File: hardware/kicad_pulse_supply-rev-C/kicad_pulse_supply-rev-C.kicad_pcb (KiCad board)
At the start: 4 copper layers, 127 x 96.5 mm, 179 parts, among them J1 USB_B_Micro, J2 SIG_EXT, J3 OPT_PWR, Q1 MMBT2222*, Q2 MMBT2222*, Q3 GAN7R0-150LBE, SW1 KMR211GLFS, U1 AP2112K-3.3, U10 LTC6244CMS8, U11 LTC6244CMS8, U12 TPS552892RYQR, U2 ESP32-WROOM-32D, U3 CP2104, U4 MAX4378, U5 UCC27611DRVT, U6 MCP1703T-5002E/MB, U7 LTC6244CMS8, U8 LTC6244CMS8, U9 LTC6244CMS8

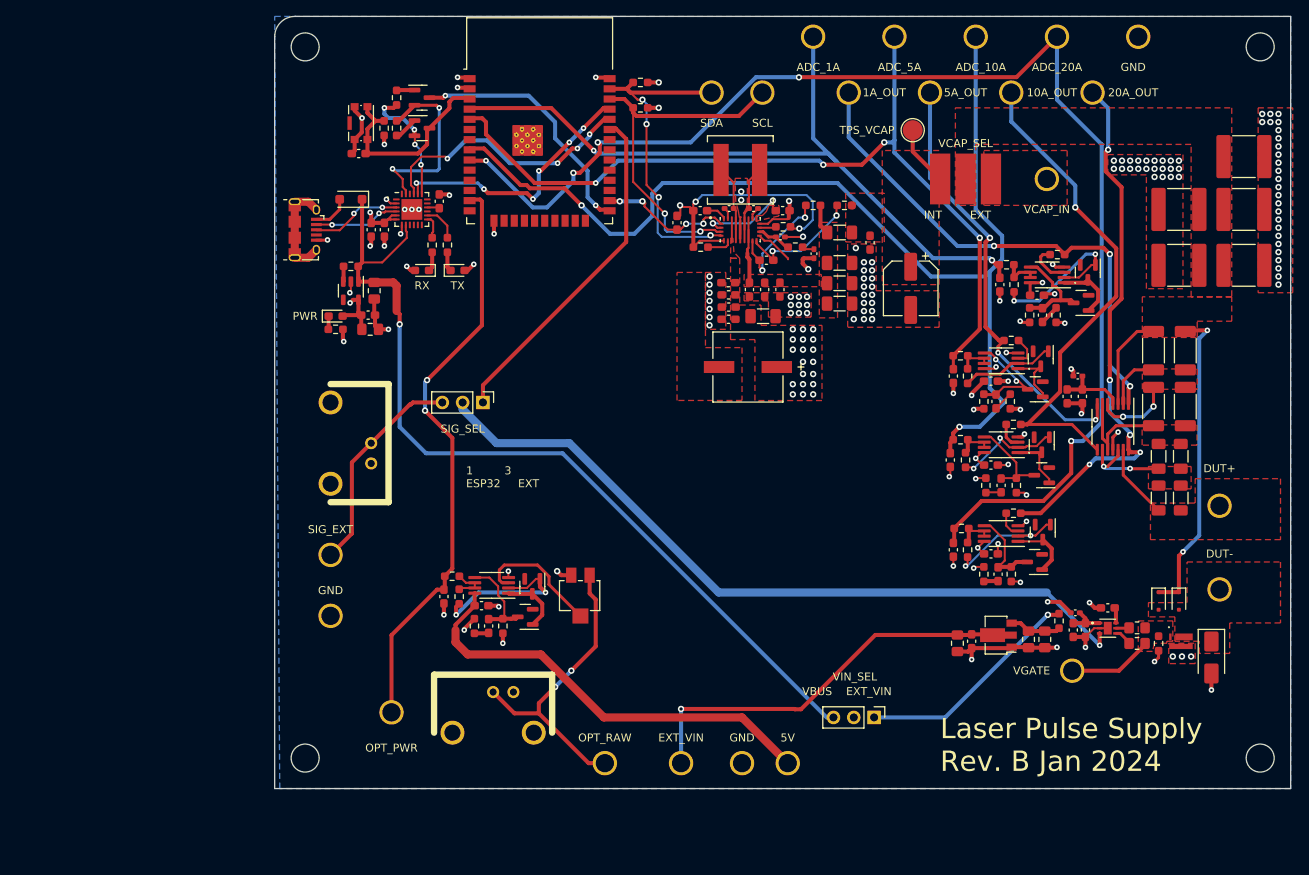
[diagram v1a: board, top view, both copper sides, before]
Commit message: Rev C pcb complete, last commit before branching firmware for new board
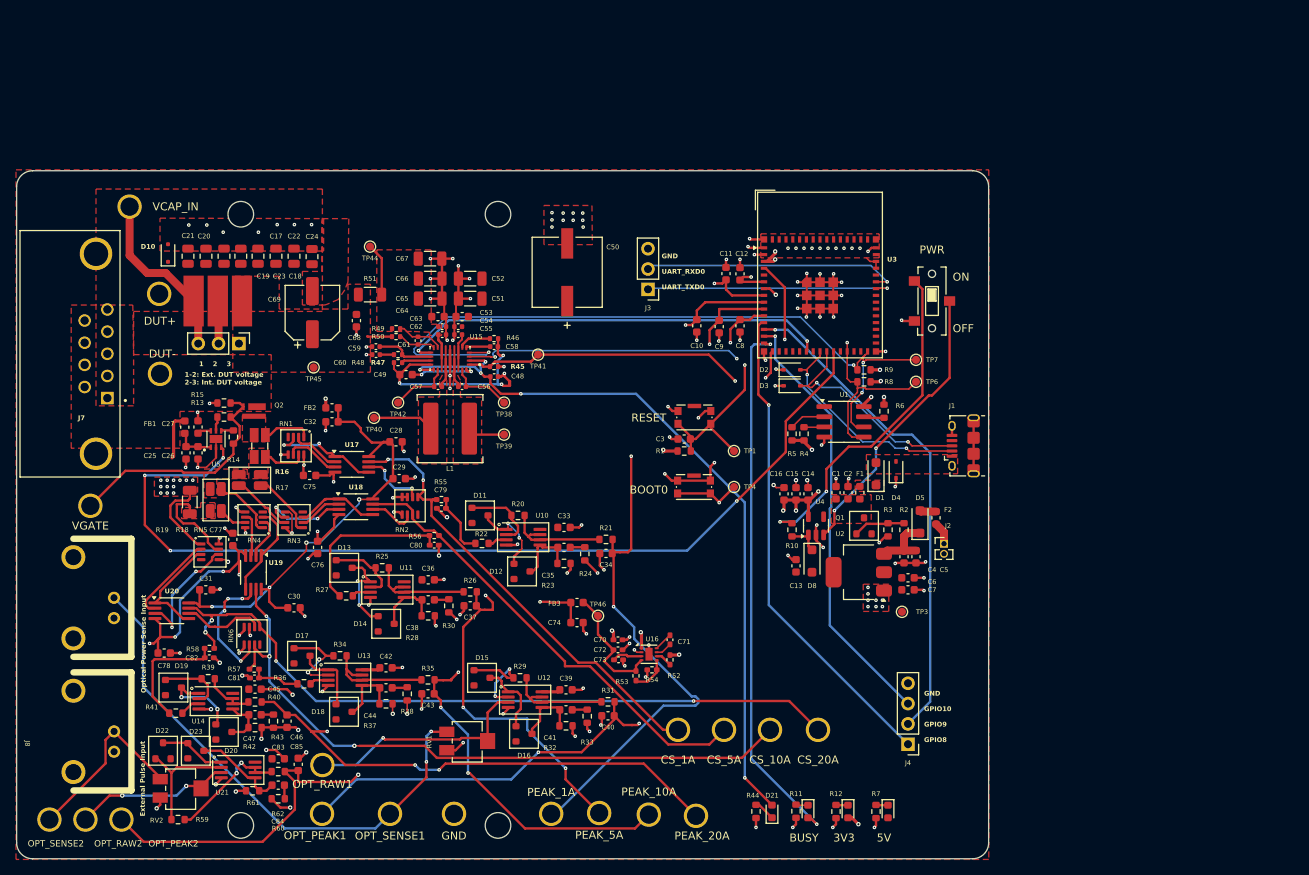
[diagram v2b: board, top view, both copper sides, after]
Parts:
- removed JP2: VIN_SEL, Connector_PinHeader_2.54mm:PinHeader_1x03_P2.54mm_Vertical
- removed JP3: VCAP_SEL, DW_Library:custom_jumper
- removed Q3: GAN7R0-150LBE, DW_Library:3-FCLGA_3.2x2.2mm
- removed TP13: 20A_OUT, DW_Library:Keystone-1502-2
- removed TP14: 5V, DW_Library:Keystone-1502-2
- removed TP15: EXT_VIN, DW_Library:Keystone-1502-2
- removed TP16: GND, DW_Library:Keystone-1502-2
- removed TP17: ADC_1A, DW_Library:Keystone-1502-2
- removed TP19: ADC_5A, DW_Library:Keystone-1502-2
- removed TP2: SDA, DW_Library:Keystone-1502-2
- removed TP20: ADC_10A, DW_Library:Keystone-1502-2
- removed TP21: ADC_20A, DW_Library:Keystone-1502-2
- removed TP23: TPS_VCAP, TestPoint:TestPoint_Pad_D2.5mm
- removed TP5: DUT+, DW_Library:Keystone-1502-2
- removed U6: MCP1703T-5002E/MB, Package_TO_SOT_SMD:SOT-89-3
- removed U7, U8, U9: LTC6244CMS8, Package_SO:MSOP-8_3x3mm_P0.65mm
- added C13: 10u, Capacitor_SMD:C_0603_1608Metric, F.Cu at (141.4, 119.5)
- added C60: 4700p, Capacitor_SMD:C_0402_1005Metric, F.Cu at (88.9, 93.1)
- added C61: 0u22, Capacitor_SMD:C_0402_1005Metric, F.Cu at (94.1, 91.3)
- added C62: 0u1, Capacitor_SMD:C_0402_1005Metric, F.Cu at (97.1, 90.6)
- added C63: 0u1, Capacitor_SMD:C_0402_1005Metric, F.Cu at (97.1, 89.6)
- added C64: 1u, Capacitor_SMD:C_0603_1608Metric, F.Cu at (96.6, 88.3)
- added C65: 10u, Capacitor_SMD:C_1206_3216Metric, F.Cu at (95.6, 86.1)
- added C66: 10u, Capacitor_SMD:C_1206_3216Metric, F.Cu at (95.6, 83.6)
- added C67: 10u, Capacitor_SMD:C_1206_3216Metric, F.Cu at (95.6, 81.1)
- added C68: 1u, Capacitor_SMD:C_0603_1608Metric, F.Cu at (86.4, 88.8)
- added C69: 100u, Capacitor_SMD:CP_Elec_6.3x5.8, F.Cu at (80.9, 87.8)
- added C70: 4u7, Capacitor_SMD:C_0402_1005Metric_Pad0.74x0.62mm_HandSolder, F.Cu at (119.1, 128.7)
- added C71: 1u, Capacitor_SMD:C_0402_1005Metric_Pad0.74x0.62mm_HandSolder, F.Cu at (125.6, 128.7)
- added C72: 4u7, Capacitor_SMD:C_0402_1005Metric_Pad0.74x0.62mm_HandSolder, F.Cu at (119.1, 130.0)
- added C73: 4u7, Capacitor_SMD:C_0402_1005Metric_Pad0.74x0.62mm_HandSolder, F.Cu at (119.2, 131.2)
- added C74: 4u7, Capacitor_SMD:C_0603_1608Metric, F.Cu at (114.0, 126.6)
- added C75: 100n, Capacitor_SMD:C_0603_1608Metric, F.Cu at (80.6, 108.2)
- added C76: 100n, Capacitor_SMD:C_0603_1608Metric, F.Cu at (81.6, 117.2)
- added C77: 100n, Capacitor_SMD:C_0603_1608Metric, F.Cu at (71.0, 116.2)
- added C78: 100n, Capacitor_SMD:C_0603_1608Metric, F.Cu at (62.4, 130.4)
- added C79: 100n, Capacitor_SMD:C_0402_1005Metric_Pad0.74x0.62mm_HandSolder, F.Cu at (97.0, 112.3)
- added C80: 100n, Capacitor_SMD:C_0402_1005Metric_Pad0.74x0.62mm_HandSolder, F.Cu at (96.1, 116.9)
- added C81: 100n, Capacitor_SMD:C_0402_1005Metric_Pad0.74x0.62mm_HandSolder, F.Cu at (73.7, 133.5)
- added C82: 100n, Capacitor_SMD:C_0402_1005Metric_Pad0.74x0.62mm_HandSolder, F.Cu at (68.0, 131.0)
- added C83: 100n, Capacitor_SMD:C_0603_1608Metric, F.Cu at (76.6, 143.6)
- added C84: 10n, Capacitor_SMD:C_0603_1608Metric, F.Cu at (76.6, 146.9)
- added C85: 1u5, Capacitor_SMD:C_0603_1608Metric, F.Cu at (79.1, 144.3)
- added D18: BAT17, PCM_Package_TO_SOT_SMD_AKL:SOT-23, F.Cu at (84.9, 137.7)
- added D19: BAT17, PCM_Package_TO_SOT_SMD_AKL:SOT-23, F.Cu at (63.5, 134.7)
- added D20: BAT17, PCM_Package_TO_SOT_SMD_AKL:SOT-23, F.Cu at (69.8, 140.2)
- added D21: RED, LED_SMD:LED_0603_1608Metric, F.Cu at (138.4, 150.2)
- added D22: BAT17, PCM_Package_TO_SOT_SMD_AKL:SOT-23, F.Cu at (62.2, 142.6)
- added D23: BAT17, PCM_Package_TO_SOT_SMD_AKL:SOT-23, F.Cu at (66.3, 142.6)
- added F1: 500mA, Fuse:Fuse_0603_1608Metric, F.Cu at (149.3, 110.3)
- added F2: 500mA, Fuse:Fuse_0603_1608Metric, F.Cu at (158.9, 113.5)
- added FB3: 330R 700mA, Capacitor_SMD:C_0603_1608Metric, F.Cu at (114.0, 124.1)
- added J4: GPIO, Connector_PinHeader_2.54mm:PinHeader_1x04_P2.54mm_Vertical, F.Cu at (155.4, 141.8)
- added J5: Conn_01x03_Pin, Connector_PinHeader_2.54mm:PinHeader_1x03_P2.54mm_Vertical, F.Cu at (71.7, 91.7)
- added J6: OPT_PWR1, DW_Library:BNC_Molex_0731375003, F.Cu at (51.0, 123.5)
- added J7: A-DF_09_A_KG-T4S, DW_Library:ASSMANN_A-DF_09_A_KG-T4S, F.Cu at (55.3, 98.5)
- added J8: OPT_PWR2, DW_Library:BNC_Molex_0731375003, F.Cu at (51.0, 140.2)
- added NT1: ~, DW_Library:Nettie-SMD-2-0.3mm, F.Cu at (119.9, 117.8)
- added NT2: ~, DW_Library:Nettie-SMD-2-0.3mm, F.Cu at (103.0, 125.0)
- added NT3: ~, DW_Library:Nettie-SMD-2-0.3mm, F.Cu at (120.4, 139.4)
- added NT4: ~, DW_Library:Nettie-SMD-2-0.3mm, F.Cu at (97.8, 133.8)
- added NT5: ~, DW_Library:Nettie-SMD-2-0.3mm, F.Cu at (81.3, 140.2)
- added NT6: ~, DW_Library:Nettie-SMD-2-0.4mm, F.Cu at (105.6, 96.7)
- added NT7: ~, DW_Library:Nettie-SMD-2-0.3mm, F.Cu at (79.6, 146.5)
- added R46: 49k9, Resistor_SMD:R_0402_1005Metric, F.Cu at (103.6, 91.1)
- added R53: 86k6, Resistor_SMD:R_0402_1005Metric_Pad0.72x0.64mm_HandSolder, F.Cu at (121.4, 133.2)
- added R54: 51k, Resistor_SMD:R_0402_1005Metric_Pad0.72x0.64mm_HandSolder, F.Cu at (123.4, 132.5)
- added R55: 0R, Resistor_SMD:R_0402_1005Metric_Pad0.72x0.64mm_HandSolder, F.Cu at (97.0, 111.2)
- added R56: 0R, Resistor_SMD:R_0402_1005Metric_Pad0.72x0.64mm_HandSolder, F.Cu at (96.1, 115.7)
- added R57: 0R, Resistor_SMD:R_0402_1005Metric_Pad0.72x0.64mm_HandSolder, F.Cu at (73.6, 132.4)
- added R58: 0R, Resistor_SMD:R_0402_1005Metric_Pad0.72x0.64mm_HandSolder, F.Cu at (68.0, 129.8)
- added R59: 2k2, Resistor_SMD:R_0603_1608Metric, F.Cu at (64.1, 151.2)
- added R60: 22, Resistor_SMD:R_0603_1608Metric, F.Cu at (76.6, 148.6)
- added R61: 1M, Resistor_SMD:R_0603_1608Metric, F.Cu at (73.4, 147.6)
- added R62: 0R, Resistor_SMD:R_0603_1608Metric, F.Cu at (76.6, 145.2)
- added RN1: RES11AXX, PCM_Package_TO_SOT_SMD_AKL:SOT-23-8, F.Cu at (78.9, 104.5)
- added RN2: RES11AXX, PCM_Package_TO_SOT_SMD_AKL:SOT-23-8, F.Cu at (93.1, 112.0)
- added RN3: RES11AXX, PCM_Package_TO_SOT_SMD_AKL:SOT-23-8, F.Cu at (78.6, 113.7)
- added RN4: RES11AXX, PCM_Package_TO_SOT_SMD_AKL:SOT-23-8, F.Cu at (73.6, 113.7)
- added RN5: RES11AXX, PCM_Package_TO_SOT_SMD_AKL:SOT-23-8, F.Cu at (68.1, 117.7)
- added RN6: RES11AXX, PCM_Package_TO_SOT_SMD_AKL:SOT-23-8, F.Cu at (73.4, 128.2)
- added RV2: 2k, Potentiometer_SMD:Potentiometer_Bourns_3214X_Vertical, F.Cu at (64.4, 147.3)
- added SW2: BOOT0, Button_Switch_SMD:SW_Push_1P1T-SH_NO_CK_KMR2xxG, F.Cu at (128.6, 109.6)
- added SW3: PWR, DW_Library:CL-SB-12B-01T, F.Cu at (158.4, 86.4)
- added TP28: CS_10A, DW_Library:Keystone-1502-2, F.Cu at (138.1, 140.0)
- added TP30: CS_20A, DW_Library:Keystone-1502-2, F.Cu at (144.1, 140.0)
- added TP31: PEAK_1A, DW_Library:Keystone-1502-2, F.Cu at (110.8, 150.5)
- added TP32: PEAK_5A, DW_Library:Keystone-1502-2, F.Cu at (116.8, 150.4)
- added TP33: OPT_PEAK1, DW_Library:Keystone-1502-2, F.Cu at (82.1, 150.5)
- added TP34: OPT_SENSE1, DW_Library:Keystone-1502-2, F.Cu at (90.6, 150.5)
- added TP35: OPT_RAW1, DW_Library:Keystone-1502-2, F.Cu at (82.2, 144.4)
- added TP36: PEAK_10A, DW_Library:Keystone-1502-2, F.Cu at (123.0, 150.6)
- added TP37: PEAK_20A, DW_Library:Keystone-1502-2, F.Cu at (128.9, 150.7)
- added TP38: ~, TestPoint:TestPoint_Pad_D1.0mm, F.Cu at (104.9, 99.1)
- added TP39: ~, TestPoint:TestPoint_Pad_D1.0mm, F.Cu at (104.9, 103.1)
- added TP40: ~, TestPoint:TestPoint_Pad_D1.0mm, F.Cu at (88.6, 101.0)
- added TP41: ~, TestPoint:TestPoint_Pad_D1.0mm, F.Cu at (109.1, 93.1)
- added TP42: ~, TestPoint:TestPoint_Pad_D1.0mm, F.Cu at (91.6, 99.1)
- added TP43: OPT_SENSE2, DW_Library:Keystone-1502-2, F.Cu at (48.0, 151.2)
- added TP44: ~, TestPoint:TestPoint_Pad_D1.0mm, F.Cu at (88.1, 79.6)
- added TP45: TPS_VCAP, TestPoint:TestPoint_Pad_D1.0mm, F.Cu at (81.1, 94.7)
- added TP46: TestPoint, TestPoint:TestPoint_Pad_D1.0mm, F.Cu at (116.6, 125.7)
- added TP47: OPT_RAW2, DW_Library:Keystone-1502-2, F.Cu at (52.5, 151.2)
- added TP48: OPT_PEAK2, DW_Library:Keystone-1502-2, F.Cu at (57.0, 151.2)
- added U13: LTC6244CMS8, PCM_Package_SO_AKL:MSOP-8_3x3mm_P0.65mm, F.Cu at (85.0, 133.5)
- added U14: LTC6244CMS8, PCM_Package_SO_AKL:MSOP-8_3x3mm_P0.65mm, F.Cu at (68.8, 136.4)
- added U15: TPS552892RYQR, DW_Library:CONV_TPS552892RYQR, F.Cu at (98.1, 93.6)
- added U16: LM27761, Package_SON:WSON-8-1EP_2x2mm_P0.5mm_EP0.9x1.6mm, F.Cu at (123.0, 130.5)
- added U17: LTC6244CMS8, Package_SO:MSOP-8_3x3mm_P0.65mm, F.Cu at (85.8, 106.8)
- added U18: LTC6244CMS8, Package_SO:MSOP-8_3x3mm_P0.65mm, F.Cu at (86.3, 112.1)
- added U19: LTC6244CMS8, Package_SO:MSOP-8_3x3mm_P0.65mm, F.Cu at (73.5, 120.3)
- added U20: LTC6244CMS8, Package_SO:MSOP-8_3x3mm_P0.65mm, F.Cu at (63.3, 125.1)
- added U21: LTC6244CMS8, PCM_Package_SO_AKL:MSOP-8_3x3mm_P0.65mm, F.Cu at (71.6, 145.0)
- C1: value 10u -> 100n; footprint Capacitor_SMD:C_0805_2012Metric_Pad1.18x1.45mm_HandSolder -> Capacitor_SMD:C_0603_1608Metric
- C10, C11, C12, C8, C9: value 47u -> 0u1; footprint Capacitor_SMD:C_2220_5650Metric -> Capacitor_SMD:C_0603_1608Metric
- C14: value 100n -> 0u1; footprint Capacitor_SMD:C_0603_1608Metric_Pad1.08x0.95mm_HandSolder -> Capacitor_SMD:C_0603_1608Metric
- C15, C16: value 1u -> 10u; footprint Capacitor_SMD:C_0603_1608Metric_Pad1.08x0.95mm_HandSolder -> Capacitor_SMD:C_0603_1608Metric
- C17, C18: value 0u1 -> 22u; footprint Capacitor_SMD:C_0603_1608Metric_Pad1.08x0.95mm_HandSolder -> Capacitor_SMD:C_0805_2012Metric
- C19, C21, C22: value 4u7 -> 22u; footprint Capacitor_SMD:C_0805_2012Metric_Pad1.18x1.45mm_HandSolder -> Capacitor_SMD:C_0805_2012Metric
- C2, C4, C6: value 0u1 -> 10u; footprint Capacitor_SMD:C_0603_1608Metric_Pad1.08x0.95mm_HandSolder -> Capacitor_SMD:C_0603_1608Metric
- C20: value 1u -> 22u; footprint Capacitor_SMD:C_0603_1608Metric_Pad1.08x0.95mm_HandSolder -> Capacitor_SMD:C_0805_2012Metric
- C23, C24: value 100n -> 22u; footprint Capacitor_SMD:C_0603_1608Metric_Pad1.08x0.95mm_HandSolder -> Capacitor_SMD:C_0805_2012Metric
- C25: value 1u5 -> 1u; footprint Capacitor_SMD:C_0603_1608Metric_Pad1.08x0.95mm_HandSolder -> Capacitor_SMD:C_0603_1608Metric
- C26: value 1u5 -> 0u1; footprint Capacitor_SMD:C_0603_1608Metric_Pad1.08x0.95mm_HandSolder -> Capacitor_SMD:C_0603_1608Metric
- C27: value 10n -> 0u1; footprint Capacitor_SMD:C_0603_1608Metric_Pad1.08x0.95mm_HandSolder -> Capacitor_SMD:C_0603_1608Metric
- C28, C31: value 10n -> 100n; footprint Capacitor_SMD:C_0603_1608Metric_Pad1.08x0.95mm_HandSolder -> Capacitor_SMD:C_0603_1608Metric
- C29, C53: footprint Capacitor_SMD:C_0603_1608Metric_Pad1.08x0.95mm_HandSolder -> Capacitor_SMD:C_0603_1608Metric
- C3: value 10u -> 0u1; footprint Capacitor_SMD:C_0805_2012Metric_Pad1.18x1.45mm_HandSolder -> Capacitor_SMD:C_0603_1608Metric
- C30, C33, C36: value 1u5 -> 100n; footprint Capacitor_SMD:C_0603_1608Metric_Pad1.08x0.95mm_HandSolder -> Capacitor_SMD:C_0603_1608Metric
- C32: value 100n -> 4u7; footprint Capacitor_SMD:C_0603_1608Metric_Pad1.08x0.95mm_HandSolder -> Capacitor_SMD:C_0603_1608Metric
- C34, C37: value 10n -> 1u5; footprint Capacitor_SMD:C_0603_1608Metric_Pad1.08x0.95mm_HandSolder -> Capacitor_SMD:C_0603_1608Metric
- C35: value 100n -> 10n; footprint Capacitor_SMD:C_0603_1608Metric_Pad1.08x0.95mm_HandSolder -> Capacitor_SMD:C_0603_1608Metric
- C38: value 4u7 -> 10n; footprint Capacitor_SMD:C_0603_1608Metric_Pad1.08x0.95mm_HandSolder -> Capacitor_SMD:C_0603_1608Metric
- C39, C42, C7: value 0u1 -> 100n; footprint Capacitor_SMD:C_0603_1608Metric_Pad1.08x0.95mm_HandSolder -> Capacitor_SMD:C_0603_1608Metric
- C40, C43: value 0u1 -> 1u5; footprint Capacitor_SMD:C_0603_1608Metric_Pad1.08x0.95mm_HandSolder -> Capacitor_SMD:C_0603_1608Metric
- C41: value 0u1 -> 10n; footprint Capacitor_SMD:C_0603_1608Metric_Pad1.08x0.95mm_HandSolder -> Capacitor_SMD:C_0603_1608Metric
- C44: value 10u -> 10n; footprint Capacitor_SMD:C_1206_3216Metric_Pad1.33x1.80mm_HandSolder -> Capacitor_SMD:C_0603_1608Metric
- C45: value 68u -> 100n; footprint DW_Library:PCAP_EEHZ_F_PAN -> Capacitor_SMD:C_0603_1608Metric
- C46: value 0u1 -> 1u5; footprint Capacitor_SMD:C_0402_1005Metric_Pad0.74x0.62mm_HandSolder -> Capacitor_SMD:C_0603_1608Metric
- C47: value 100p -> 10n; footprint Capacitor_SMD:C_0402_1005Metric_Pad0.74x0.62mm_HandSolder -> Capacitor_SMD:C_0603_1608Metric
- C48: value 4700p -> 0u1; footprint Capacitor_SMD:C_0402_1005Metric_Pad0.74x0.62mm_HandSolder -> Capacitor_SMD:C_0402_1005Metric
- C49: value 0u1 -> 4u7; footprint Capacitor_SMD:C_0402_1005Metric_Pad0.74x0.62mm_HandSolder -> Capacitor_SMD:C_0603_1608Metric
- C5: value 1u -> 100n; footprint Capacitor_SMD:C_0603_1608Metric_Pad1.08x0.95mm_HandSolder -> Capacitor_SMD:C_0603_1608Metric
- C50: value 0u22 -> 68u; footprint Capacitor_SMD:C_0603_1608Metric_Pad1.08x0.95mm_HandSolder -> DW_Library:PCAP_EEHZ_F_PAN
- C51, C52: value 0u1 -> 10u; footprint Capacitor_SMD:C_0603_1608Metric_Pad1.08x0.95mm_HandSolder -> Capacitor_SMD:C_1206_3216Metric
- C54, C55, C56: value 10u -> 0u1; footprint Capacitor_SMD:C_1206_3216Metric_Pad1.33x1.80mm_HandSolder -> Capacitor_SMD:C_0402_1005Metric
- C57: value 1u -> 0u1; footprint Capacitor_SMD:C_0603_1608Metric_Pad1.08x0.95mm_HandSolder -> Capacitor_SMD:C_0402_1005Metric
- C58: value 100u -> 0u01; footprint Capacitor_SMD:CP_Elec_6.3x5.8 -> Capacitor_SMD:C_0402_1005Metric
- C59: value 0u1 -> 100p; footprint Capacitor_SMD:C_0603_1608Metric_Pad1.08x0.95mm_HandSolder -> Capacitor_SMD:C_0402_1005Metric
- D1: value PWR -> MBR120; footprint LED_SMD:LED_0603_1608Metric_Pad1.05x0.95mm_HandSolder -> Diode_SMD:D_SOD-123F
- D10: value BAT17 -> 24V 550mW; footprint Package_TO_SOT_SMD:SOT-23 -> Diode_SMD:D_SOD-323F
- D11, D12, D13, D14, D15, D16, D17: footprint Package_TO_SOT_SMD:SOT-23 -> PCM_Package_TO_SOT_SMD_AKL:SOT-23
- D2: value MBR120 -> 5VWM; footprint Diode_SMD:D_SOD-123F -> Diode_SMD:D_SOD-323
- D3: value TX -> 5VWM; footprint LED_SMD:LED_0603_1608Metric_Pad1.05x0.95mm_HandSolder -> Diode_SMD:D_SOD-323
- D4: value RX -> 5VWM; footprint LED_SMD:LED_0603_1608Metric_Pad1.05x0.95mm_HandSolder -> Diode_SMD:D_SOD-323
- D5: value 100V 200mA -> MBR120; footprint Diode_SMD:D_SOD-323F -> Diode_SMD:D_SOD-123F
- D6: value 100V 200mA -> 5V; footprint Diode_SMD:D_SOD-323F -> LED_SMD:LED_0603_1608Metric
- D7: value 24V 1W -> BUSY; footprint Diode_SMD:D_SMA -> LED_SMD:LED_0603_1608Metric
- D8: value BAT17 -> MBR120; footprint Package_TO_SOT_SMD:SOT-23 -> Diode_SMD:D_SOD-123F
- D9: value BAT17 -> 3V3; footprint Package_TO_SOT_SMD:SOT-23 -> LED_SMD:LED_0603_1608Metric
- FB1, FB2: footprint Capacitor_SMD:C_0402_1005Metric_Pad0.74x0.62mm_HandSolder -> Capacitor_SMD:C_0603_1608Metric
- H1, H2, H3, H4: footprint MountingHole:MountingHole_3.5mm -> MountingHole:MountingHole_3.2mm_M3
- J1: footprint DW_Library:USB_Micro-B_Amphenol_10118194_Horizontal -> Connector_USB:USB_Micro-B_Amphenol_10118194_Horizontal
- J2: value SIG_EXT -> PWR; footprint DW_Library:BNC_Molex_0731375003 -> Connector_PinHeader_1.27mm:PinHeader_1x02_P1.27mm_Vertical
- J3: value OPT_PWR -> UART TX RX; footprint DW_Library:BNC_Molex_0731375003 -> Connector_PinHeader_2.54mm:PinHeader_1x03_P2.54mm_Vertical
- JP1: value SIG_SEL -> VCAP_SEL; footprint Connector_PinHeader_2.54mm:PinHeader_1x03_P2.54mm_Vertical -> DW_Library:custom_jumper
- Q1: value MMBT2222* -> DMG3415U; footprint Package_TO_SOT_SMD:SOT-23 -> PCM_Package_TO_SOT_SMD_AKL:SOT-23
- Q2: value MMBT2222* -> GAN7R0-150LBE; footprint Package_TO_SOT_SMD:SOT-23 -> DW_Library:3-FCLGA_3.2x2.2mm
- R1, R28, R3, R30: footprint Resistor_SMD:R_0603_1608Metric_Pad0.98x0.95mm_HandSolder -> Resistor_SMD:R_0603_1608Metric
- R10: value 0R3 -> 100k; footprint Resistor_SMD:R_2010_5025Metric_Pad1.40x2.65mm_HandSolder -> Resistor_SMD:R_0603_1608Metric
- R11: value 0R3 -> 500R; footprint Resistor_SMD:R_2010_5025Metric_Pad1.40x2.65mm_HandSolder -> Resistor_SMD:R_0603_1608Metric
- R12: value 10 -> 500R; footprint Resistor_SMD:R_0805_2012Metric_Pad1.20x1.40mm_HandSolder -> Resistor_SMD:R_0603_1608Metric
- R13: footprint Resistor_SMD:R_0805_2012Metric_Pad1.20x1.40mm_HandSolder -> Resistor_SMD:R_0603_1608Metric
- R14: value 10k -> 10; footprint Resistor_SMD:R_0603_1608Metric_Pad0.98x0.95mm_HandSolder -> Resistor_SMD:R_0603_1608Metric
- R15: value 0R06 -> 10k; footprint Resistor_SMD:R_2010_5025Metric_Pad1.40x2.65mm_HandSolder -> Resistor_SMD:R_0603_1608Metric
- R16: value 0R06 -> 0R1; footprint Resistor_SMD:R_2010_5025Metric_Pad1.40x2.65mm_HandSolder -> Resistor_SMD:R_Shunt_Ohmite_LVK12
- R17: value 0R03 -> 0R02; footprint Resistor_SMD:R_1206_3216Metric_Pad1.30x1.75mm_HandSolder -> PCM_Resistor_SMD_AKL:R_Shunt_Ohmite_LVK12
- R18: value 0R03 -> 0R01; footprint Resistor_SMD:R_1206_3216Metric_Pad1.30x1.75mm_HandSolder -> PCM_Resistor_SMD_AKL:R_Shunt_Ohmite_LVK12
- R19: value 0R015 -> 0R005; footprint Resistor_SMD:R_1206_3216Metric_Pad1.30x1.75mm_HandSolder -> Resistor_SMD:R_1206_3216Metric
- R2: value 10k -> 100k; footprint Resistor_SMD:R_0603_1608Metric_Pad0.98x0.95mm_HandSolder -> Resistor_SMD:R_0603_1608Metric
- R20: value 0R015 -> 2k2; footprint Resistor_SMD:R_1206_3216Metric_Pad1.30x1.75mm_HandSolder -> Resistor_SMD:R_0603_1608Metric
- R21: value 0 -> 0R; footprint Resistor_SMD:R_0603_1608Metric_Pad0.98x0.95mm_HandSolder -> Resistor_SMD:R_0603_1608Metric
- R22, R36, R41: value 2k2 -> 1k; footprint Resistor_SMD:R_0603_1608Metric_Pad0.98x0.95mm_HandSolder -> Resistor_SMD:R_0603_1608Metric
- R23: value 2k2 -> 1M; footprint Resistor_SMD:R_0603_1608Metric_Pad0.98x0.95mm_HandSolder -> Resistor_SMD:R_0603_1608Metric
- R24: value 10k -> 22; footprint Resistor_SMD:R_0603_1608Metric_Pad0.98x0.95mm_HandSolder -> Resistor_SMD:R_0603_1608Metric
- R25: value 10k -> 2k2; footprint Resistor_SMD:R_0603_1608Metric_Pad0.98x0.95mm_HandSolder -> Resistor_SMD:R_0603_1608Metric
- R26, R4: value 1k -> 0R; footprint Resistor_SMD:R_0603_1608Metric_Pad0.98x0.95mm_HandSolder -> Resistor_SMD:R_0603_1608Metric
- R27, R44: value 1M -> 1k; footprint Resistor_SMD:R_0603_1608Metric_Pad0.98x0.95mm_HandSolder -> Resistor_SMD:R_0603_1608Metric
- R29: value 22 -> 2k2; footprint Resistor_SMD:R_0603_1608Metric_Pad0.98x0.95mm_HandSolder -> Resistor_SMD:R_0603_1608Metric
- R31, R6: value 2k2 -> 0R; footprint Resistor_SMD:R_0603_1608Metric_Pad0.98x0.95mm_HandSolder -> Resistor_SMD:R_0603_1608Metric
- R32, R37, R42: value 10k -> 1M; footprint Resistor_SMD:R_0603_1608Metric_Pad0.98x0.95mm_HandSolder -> Resistor_SMD:R_0603_1608Metric
- R33, R38, R43: value 1k -> 22; footprint Resistor_SMD:R_0603_1608Metric_Pad0.98x0.95mm_HandSolder -> Resistor_SMD:R_0603_1608Metric
- R34, R39: value 1M -> 2k2; footprint Resistor_SMD:R_0603_1608Metric_Pad0.98x0.95mm_HandSolder -> Resistor_SMD:R_0603_1608Metric
- R35, R40: value 22 -> 0R; footprint Resistor_SMD:R_0603_1608Metric_Pad0.98x0.95mm_HandSolder -> Resistor_SMD:R_0603_1608Metric
- R45: value 22 -> 2k; footprint Resistor_SMD:R_0603_1608Metric_Pad0.98x0.95mm_HandSolder -> Resistor_SMD:R_0402_1005Metric
- R47: value 27k4 -> 150k; footprint Resistor_SMD:R_0603_1608Metric_Pad0.98x0.95mm_HandSolder -> Resistor_SMD:R_0402_1005Metric
- R48: value 49k9 -> 27k4; footprint Resistor_SMD:R_0603_1608Metric_Pad0.98x0.95mm_HandSolder -> Resistor_SMD:R_0402_1005Metric
- R49: value 150k -> 10; footprint Resistor_SMD:R_0603_1608Metric_Pad0.98x0.95mm_HandSolder -> Resistor_SMD:R_0402_1005Metric
- R5: value 10k -> 0R; footprint Resistor_SMD:R_0603_1608Metric_Pad0.98x0.95mm_HandSolder -> Resistor_SMD:R_0603_1608Metric
- R50: footprint Resistor_SMD:R_0603_1608Metric_Pad0.98x0.95mm_HandSolder -> Resistor_SMD:R_0402_1005Metric
- R51: value 10 -> 10m; footprint Resistor_SMD:R_0603_1608Metric_Pad0.98x0.95mm_HandSolder -> Resistor_SMD:R_1206_3216Metric
- R52: value 10m -> 2k; footprint Resistor_SMD:R_1206_3216Metric_Pad1.30x1.75mm_HandSolder -> Resistor_SMD:R_0402_1005Metric_Pad0.72x0.64mm_HandSolder
- R7: value 2k2 -> 1k2; footprint Resistor_SMD:R_0603_1608Metric_Pad0.98x0.95mm_HandSolder -> Resistor_SMD:R_0603_1608Metric
- R8, R9: value 1k -> 2k2; footprint Resistor_SMD:R_0603_1608Metric_Pad0.98x0.95mm_HandSolder -> Resistor_SMD:R_0603_1608Metric
- SW1: value KMR211GLFS -> RESET
- TP1: value SCL -> ~; footprint DW_Library:Keystone-1502-2 -> TestPoint:TestPoint_Pad_D1.0mm
- TP10: value GND -> DUT+
- TP11: value 5A_OUT -> DUT-
- TP12: value 10A_OUT -> VGATE
- TP18: value OPT_PEAK -> CS_1A
- TP22: value OPT_RAW -> CS_5A
- TP3: value VCAP_IN -> ~; footprint DW_Library:Keystone-1502-2 -> TestPoint:TestPoint_Pad_D1.0mm
- TP4: value GND -> ~; footprint DW_Library:Keystone-1502-2 -> TestPoint:TestPoint_Pad_D1.0mm
- TP6: value VGATE -> ~; footprint DW_Library:Keystone-1502-2 -> TestPoint:TestPoint_Pad_D1.0mm
- TP7: value DUT- -> ~; footprint DW_Library:Keystone-1502-2 -> TestPoint:TestPoint_Pad_D1.0mm
- TP8: value 1A_OUT -> VCAP_IN
- TP9: value SIG_EXT -> GND
- U1: value AP2112K-3.3 -> CY15B004J; footprint Package_TO_SOT_SMD:SOT-23-5 -> Package_SO:SOIC-8_3.9x4.9mm_P1.27mm
- U10, U11: footprint Package_SO:MSOP-8_3x3mm_P0.65mm -> PCM_Package_SO_AKL:MSOP-8_3x3mm_P0.65mm
- U12: value TPS552892RYQR -> LTC6244CMS8; footprint DW_Library:CONV_TPS552892RYQR -> PCM_Package_SO_AKL:MSOP-8_3x3mm_P0.65mm
- U2: value ESP32-WROOM-32D -> NCP1117-5.0_SOT223; footprint RF_Module:ESP32-WROOM-32D -> Package_TO_SOT_SMD:SOT-223-3_TabPin2
- U3: value CP2104 -> ESP32-S3-MINI-1; footprint Package_DFN_QFN:QFN-24-1EP_4x4mm_P0.5mm_EP2.6x2.6mm -> DW_Library:ESP32-S2-MINI-1
- U4: value MAX4378 -> AP2112K-3.3; footprint Package_SO:TSSOP-14_4.4x5mm_P0.65mm -> Package_TO_SOT_SMD:SOT-23-5
- moved TP12 126.2 mm to (53.2, 112.0)
- moved R19 123.9 mm to (65.6, 111.5), turned to 90 degrees
- moved R15 120.2 mm to (69.9, 99.1), turned to 180 degrees
- moved R14 118.5 mm to (71.0, 103.4)
- moved R18 118.0 mm to (68.8, 111.3), turned to 0 degrees
- moved R13 117.6 mm to (69.9, 100.9)
- moved R17 116.4 mm to (73.1, 108.8)
- moved C21 115.5 mm to (65.4, 80.8), turned to 90 degrees
- moved C18 115.0 mm to (74.1, 80.8), turned to 90 degrees
- moved D10 114.3 mm to (62.9, 80.4), turned to 90 degrees
- moved U5 114.0 mm to (68.9, 103.6), turned to 90 degrees
- moved R16 111.8 mm to (74.3, 104.5), turned to 0 degrees
- moved FB1 111.8 mm to (65.0, 102.1), turned to -90 degrees
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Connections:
- C10 pad 1: VCAP -> ESP_ADC1_CH4
- C11 pad 1: VCAP -> ESP_ADC1_CH3
- C12 pad 1: VCAP -> ESP_ADC1_CH1
- C14 pad 1: GND -> +3V3
- C14 pad 2: Net-(U4A-VCC) -> GND
- C15 pad 1: GND -> +3V3
- C15 pad 2: Net-(U4A-VCC) -> GND
- C16 pad 1: Net-(U5-VDD) -> +3V3
- C17 pad 1: Net-(U5-VDD) -> /Switching FET/DUT+
- C18 pad 1: /GaN FET and Current Sensing/vref -> /Switching FET/DUT+
- C19 pad 1: VIN -> /Switching FET/DUT+
- C2 pad 1: +3V3 -> VBUS
- C20 pad 1: VIN -> /Switching FET/DUT+
- C21 pad 1: /GaN FET and Current Sensing/vout_5v -> /Switching FET/DUT+
- C22 pad 1: /GaN FET and Current Sensing/vout_5v -> /Switching FET/DUT+
- C23 pad 1: +5V -> /Switching FET/DUT+
- C24 pad 1: +5V -> /Switching FET/DUT+
- C25 pad 1: ADC_1A -> Net-(U5-VDD)
- C26 pad 1: OPT_IN_ADC -> Net-(U5-VDD)
- C27 pad 1: Net-(D10-K) -> /Switching FET/vref
- C27 pad 2: Net-(C27-Pad2) -> GND
- C28 pad 1: Net-(D11-K) -> /Current Sensing/3V3_FB
- C28 pad 2: Net-(C28-Pad2) -> GND
- C29 pad 1: +5V -> /Current Sensing/3V3_FB
- C3 pad 1: +3V3 -> /ESP32/RESET
- C30 pad 1: ADC_5A -> /Current Sensing/3V3_FB
- C31 pad 1: Net-(D13-K) -> /Current Sensing/3V3_FB
- C31 pad 2: Net-(C31-Pad2) -> GND
- C32 pad 1: +5V -> GND
- C32 pad 2: GND -> /Current Sensing/3V3_FB
- C33 pad 1: ADC_10A -> +5V
- C34 pad 1: Net-(D15-K) -> Net-(C34-Pad1)
- C34 pad 2: Net-(C34-Pad2) -> GND
- C35 pad 1: +5V -> Net-(D12-K)
- C35 pad 2: GND -> Net-(C35-Pad2)
- C36 pad 1: ADC_20A -> +5V
- C37 pad 1: Net-(D17-K) -> Net-(C37-Pad1)
- C37 pad 2: Net-(C37-Pad2) -> GND
- C38 pad 1: /Buck Boost Supply/Vcc -> Net-(D14-K)
- C38 pad 2: GND -> Net-(C38-Pad2)
- C39 pad 1: /Buck Boost Supply/Vcc -> +5V
- C4 pad 1: /ESP32/RESET -> VIN
- C40 pad 1: +5V -> /Peak Detection/PEAK_OPT1
- C41 pad 1: +5V -> Net-(D16-K)
- C41 pad 2: GND -> Net-(C41-Pad2)
- C43 pad 1: +5V -> Net-(C43-Pad1)
- C44 pad 1: +5V -> Net-(D18-K)
- C44 pad 2: GND -> Net-(C44-Pad2)
- C46 pad 1: /Buck Boost Supply/SW1 -> Net-(C46-Pad1)
- C46 pad 2: /Buck Boost Supply/BOOT1 -> GND
- C47 pad 1: /Buck Boost Supply/COMP -> Net-(D20-K)
- C47 pad 2: GND -> Net-(C47-Pad2)
- C48 pad 1: Net-(C48-Pad1) -> /I2C Voltage Supply/VCC
- C49 pad 1: /Buck Boost Supply/SW2 -> Net-(U15-EXTVCC)
- C49 pad 2: /Buck Boost Supply/BOOT2 -> GNDA
- C5 pad 1: +3V3 -> VIN
- C50 pad 1: /Buck Boost Supply/ISN -> +5V
- C50 pad 2: /Buck Boost Supply/ISP -> GND
- C51 pad 1: /Buck Boost Supply/Vout -> +5V
- C52 pad 1: /Buck Boost Supply/Vout -> +5V
- C53 pad 1: /Buck Boost Supply/Vout -> +5V
- C54 pad 1: /Buck Boost Supply/Vout -> +5V
- C55 pad 1: /Buck Boost Supply/Vout -> +5V
- C56 pad 1: /Buck Boost Supply/Vout -> /I2C Voltage Supply/SW1
- C56 pad 2: GND -> /I2C Voltage Supply/BOOT1
- C57 pad 1: /Buck Boost Supply/tps_out -> /I2C Voltage Supply/SW2
- C57 pad 2: GND -> /I2C Voltage Supply/BOOT2
- C58 pad 1: /Buck Boost Supply/tps_out -> Net-(U15-DITH/SYNC)
- C58 pad 2: GND -> GNDA
- C59 pad 1: EN/UVLO -> /I2C Voltage Supply/COMP
- C6 pad 1: +3V3 -> +5V
- C7 pad 1: Net-(U3-VPP) -> +5V
- C8 pad 1: VCAP -> ESP_ADC1_CH6
- C9 pad 1: VCAP -> ESP_ADC1_CH5
- D1 pad 2: +3V3 -> Net-(D1-A)
- D10 pad 1: Net-(D10-A) -> /Switching FET/DUT+
- D10 pad 2: unconnected-(D10-NC-Pad2) -> GND
- D12 pad 1: Net-(D12-A) -> Net-(D11-K)
- D13 pad 1: Net-(D12-K) -> Net-(D13-A)
- D14 pad 1: Net-(D14-A) -> Net-(D13-K)
- D15 pad 1: Net-(D14-K) -> Net-(D15-A)
- D16 pad 1: Net-(D16-A) -> Net-(D15-K)
- D17 pad 1: Net-(D16-K) -> Net-(D17-A)
- D2 pad 1: VBUS -> GND
- D2 pad 2: Net-(D2-A) -> /ESP32/USB_D-
- D3 pad 1: Net-(D3-K) -> GND
- D3 pad 2: +3V3 -> /ESP32/USB_D+
- D4 pad 1: Net-(D4-K) -> GND
- D4 pad 2: +3V3 -> Net-(D1-A)
- D5 pad 1: VCAP -> VIN
- D6 pad 1: VCAP -> Net-(D6-K)
- D6 pad 2: Net-(D5-A) -> +5V
- D7 pad 1: Net-(D5-A) -> Net-(D7-K)
- D7 pad 2: GND -> Net-(D7-A)
- D8 pad 1: Net-(D8-A) -> Net-(D8-K)
- D8 pad 2: unconnected-(D8-NC-Pad2) -> +5V
- D9 pad 1: Net-(D9-A) -> Net-(D9-K)
- D9 pad 2: unconnected-(D9-NC-Pad2) -> +3V3
- FB1 pad 1: +3V3 -> +5V
- FB1 pad 2: Net-(U4A-VCC) -> Net-(U5-VDD)
- FB2 pad 1: +5V -> +3V3
- FB2 pad 2: Net-(U5-VDD) -> /Current Sensing/3V3_FB
- J1 pad 1: Net-(D2-A) -> Net-(D1-A)
- J1 pad 2: /ESP32/d- -> /ESP32/USB_D-
- J1 pad 3: /ESP32/d+ -> /ESP32/USB_D+
- J1 pad 6: unconnected-(J1-Shield-Pad6) -> GND
- J2 pad 1: /GaN FET and Current Sensing/sig_ext -> Net-(J2-Pin_1)
- J3 pad 1: Net-(J3-In) -> /ESP32/TXD0
- J3 pad 2: GND -> /ESP32/RXD0
- JP1 pad 1: PULSE_IN -> TPS_VCAP
- JP1 pad 2: /GaN FET and Current Sensing/in+ -> /Switching FET/DUT+
- JP1 pad 3: /GaN FET and Current Sensing/sig_ext -> Net-(J5-Pin_3)
- L1 pad 1: /Buck Boost Supply/SW1 -> /I2C Voltage Supply/SW1
- L1 pad 2: /Buck Boost Supply/SW2 -> /I2C Voltage Supply/SW2
- Q1 pad 1: Net-(Q1-Pad1) -> Net-(Q1-G)
- Q1 pad 2: /ESP32/DTR -> +5V
- Q1 pad 3: /ESP32/GPIO0 -> VBUS
- Q2 pad 1: Net-(Q2-Pad1) -> /Switching FET/vgate
- Q2 pad 2: /ESP32/RTS -> CS_IN
- Q2 pad 3: /ESP32/RESET -> /Switching FET/ DUT-
- R1 pad 1: /ESP32/RTS -> /ESP32/RESET
- R1 pad 2: Net-(Q1-Pad1) -> +3V3
- R10 pad 1: VCAP -> Net-(D8-K)
- R10 pad 2: Net-(U4A--) -> Net-(R10-Pad2)
- R11 pad 1: VCAP -> GND
- R11 pad 2: Net-(U4A--) -> Net-(D7-K)
- R12 pad 1: /GaN FET and Current Sensing/OUTH -> GND
- R12 pad 2: /GaN FET and Current Sensing/vgate -> Net-(D9-K)
- R13 pad 1: /GaN FET and Current Sensing/OUTL -> /Switching FET/OUTH
- R13 pad 2: /GaN FET and Current Sensing/vgate -> /Switching FET/vgate
- R14 pad 1: /GaN FET and Current Sensing/vgate -> /Switching FET/OUTL
- R14 pad 2: GND -> /Switching FET/vgate
- R15 pad 1: Net-(U4A--) -> /Switching FET/vgate
- R15 pad 2: Net-(U4B--) -> GND
- R16 pad 1: Net-(U4A--) -> CS_IN
- R16 pad 2: Net-(U4B--) -> Net-(RN1A-RIN1)
- R17 pad 1: Net-(U4B--) -> Net-(R16-Pad4)
- R17 pad 2: Net-(U4C--) -> Net-(RN3A-RIN1)
- R18 pad 1: Net-(U4B--) -> Net-(R17-Pad4)
- R18 pad 2: Net-(U4C--) -> Net-(RN4A-RIN1)
- R19 pad 1: Net-(U4C--) -> Net-(RN5B-RIN2)
- R19 pad 2: /GaN FET and Current Sensing/sense_out -> GND
- R2 pad 1: /ESP32/RESET -> Net-(Q1-G)
- R2 pad 2: +3V3 -> VIN
- R20 pad 1: Net-(U4C--) -> Net-(D11-A)
- R20 pad 2: /GaN FET and Current Sensing/sense_out -> Net-(U10B--)
- R21 pad 1: Net-(JP2-A) -> Net-(U10B--)
- R21 pad 2: /GaN FET and Current Sensing/vout_5v -> Net-(C34-Pad1)
- R22 pad 1: Net-(D8-A) -> CS_1A
- R22 pad 2: Net-(U7B--) -> Net-(U10A-+)
- R23 pad 1: Net-(D9-A) -> Net-(D12-K)
- R23 pad 2: Net-(U8B--) -> GND
- R24 pad 1: Net-(U7B--) -> Net-(C35-Pad2)
- R24 pad 2: ADC_1A -> GND
- R25 pad 1: Net-(U8B--) -> Net-(D13-A)
- R25 pad 2: OPT_IN_ADC -> Net-(U11B--)
- R26 pad 1: SENSE_1A -> Net-(U11B--)
- R26 pad 2: Net-(U7A-+) -> Net-(C37-Pad1)
- R27 pad 1: Net-(D10-K) -> CS_5A
- R27 pad 2: GND -> Net-(U11A-+)
- R28 pad 1: Net-(D11-K) -> Net-(D14-K)
- R29 pad 1: Net-(C27-Pad2) -> Net-(D15-A)
- R29 pad 2: GND -> Net-(U12B--)
- R3 pad 1: VBUS -> Net-(Q1-G)
- R3 pad 2: Net-(U1-EN) -> GND
- R30 pad 1: Net-(C28-Pad2) -> Net-(C38-Pad2)
- R31 pad 1: Net-(D12-A) -> Net-(U12B--)
- R31 pad 2: Net-(U9B--) -> /Peak Detection/PEAK_OPT1
- R32 pad 1: Net-(U9B--) -> Net-(D16-K)
- R32 pad 2: ADC_5A -> GND
- R33 pad 1: SENSE_5A -> Net-(C41-Pad2)
- R33 pad 2: Net-(U9A-+) -> GND
- R34 pad 1: Net-(D13-K) -> Net-(D17-A)
- R34 pad 2: GND -> Net-(U13B--)
- R35 pad 1: Net-(C31-Pad2) -> Net-(U13B--)
- R35 pad 2: GND -> Net-(C43-Pad1)
- R36 pad 1: Net-(D14-A) -> CS_10A
- R36 pad 2: Net-(U10B--) -> Net-(U13A-+)
- R37 pad 1: Net-(U10B--) -> Net-(D18-K)
- R37 pad 2: ADC_10A -> GND
- R38 pad 1: SENSE_10A -> Net-(C44-Pad2)
- R38 pad 2: Net-(U10A-+) -> GND
- R39 pad 1: Net-(D15-K) -> Net-(D19-A)
- R39 pad 2: GND -> Net-(U14B--)
- R4 pad 1: GND -> +3V3
- R4 pad 2: Net-(D1-K) -> Net-(U1-A2)
- R40 pad 1: Net-(C34-Pad2) -> Net-(U14B--)
- R40 pad 2: GND -> Net-(C46-Pad1)
- R41 pad 1: Net-(D16-A) -> CS_20A
- R41 pad 2: Net-(U11B--) -> Net-(U14A-+)
- R42 pad 1: Net-(U11B--) -> Net-(D20-K)
- R42 pad 2: ADC_20A -> GND
- R43 pad 1: SENSE_20A -> Net-(C47-Pad2)
- R43 pad 2: Net-(U11A-+) -> GND
- R44 pad 1: Net-(D17-K) -> Net-(D21-K)
- R45 pad 1: Net-(C37-Pad2) -> EN/UVLO
- R47 pad 1: /Buck Boost Supply/COMP -> Net-(U15-CDC)
- R47 pad 2: Net-(C48-Pad1) -> GNDA
- R48 pad 1: Net-(U12-FSW) -> /I2C Voltage Supply/COMP
- R48 pad 2: GND -> Net-(C60-Pad1)
- R49 pad 1: Net-(U12-CDC) -> /I2C Voltage Supply/ISP
- R49 pad 2: GND -> /I2C Voltage Supply/VOUT
- R5 pad 1: /ESP32/DTR -> +3V3
- R5 pad 2: Net-(Q2-Pad1) -> Net-(U1-A1)
- R50 pad 1: /Buck Boost Supply/ISP -> /I2C Voltage Supply/ISN
- R50 pad 2: /Buck Boost Supply/Vout -> TPS_VCAP
- R51 pad 1: /Buck Boost Supply/ISN -> /I2C Voltage Supply/VOUT
- R51 pad 2: /Buck Boost Supply/tps_out -> TPS_VCAP
- R52 pad 1: /Buck Boost Supply/Vout -> +3V3
- R52 pad 2: /Buck Boost Supply/tps_out -> /Current Sensing/EN
- R6 pad 1: SCL -> +3V3
- R6 pad 2: +3V3 -> Net-(U1-WP)
- R7 pad 1: SDA -> GND
- R7 pad 2: +3V3 -> Net-(D6-K)
- R8 pad 1: Net-(U3-TXT/GPIO.0) -> SDA
- R8 pad 2: Net-(D3-K) -> +3V3
- R9 pad 1: Net-(U3-RXT/GPIO.1) -> SCL
- R9 pad 2: Net-(D4-K) -> +3V3
- RV1 pad 1: Net-(J3-In) -> Net-(J6-In)
- RV1 pad 2: Net-(U8A-+) -> Net-(U12A-+)
- TP1 pad 1: SCL -> /ESP32/RESET
- TP10 pad 1: GND -> /Switching FET/DUT+
- TP11 pad 1: SENSE_5A -> /Switching FET/ DUT-
- TP12 pad 1: SENSE_10A -> /Switching FET/vgate
- TP18 pad 1: OPT_IN_ADC -> Net-(RN2B-RG2)
- TP22 pad 1: Net-(J3-In) -> Net-(RN2A-RG1)
- TP3 pad 1: VCAP_EXT -> +5V
- TP4 pad 1: GND -> /ESP32/BOOT0
- TP6 pad 1: /GaN FET and Current Sensing/vgate -> SDA
- TP7 pad 1: Net-(D5-A) -> SCL
- TP8 pad 1: SENSE_1A -> Net-(J5-Pin_3)
- TP9 pad 1: /GaN FET and Current Sensing/sig_ext -> GND
- U1 pad 1: VBUS -> unconnected-(U1-NC-Pad1)
- U1 pad 2: GND -> Net-(U1-A1)
- U1 pad 3: Net-(U1-EN) -> Net-(U1-A2)
- U1 pad 4: unconnected-(U1-NC-Pad4) -> GND
- U1 pad 5: +3V3 -> SDA
- U10 pad 1: Net-(D14-K) -> Net-(D11-K)
- U10 pad 2: Net-(D14-A) -> Net-(D11-A)
- U10 pad 5: Net-(D15-K) -> Net-(D12-K)
- U11 pad 1: Net-(D16-K) -> Net-(D13-K)
- U11 pad 2: Net-(D16-A) -> Net-(D13-A)
- U11 pad 5: Net-(D17-K) -> Net-(D14-K)
- U12 pad 1: EN/UVLO -> Net-(D15-K)
- U12 pad 2: /Buck Boost Supply/Vcc -> Net-(D15-A)
- U12 pad 3: SCL -> Net-(U12A-+)
- U12 pad 4: SDA -> GND
- U12 pad 5: GND -> Net-(D16-K)
- U12 pad 6: Net-(U12-FSW) -> Net-(U12B--)
- U12 pad 7: +5V -> Net-(U12B--)
- U12 pad 8: /Buck Boost Supply/SW1 -> +5V
- U2 pad 2: +3V3 -> +5V
- U2 pad 3: /ESP32/RESET -> VIN
- U3 pad 1: unconnected-(U3-~{RI}-Pad1) -> GND
- U3 pad 10: unconnected-(U3-NC-Pad10) -> ESP_ADC1_CH5
- U3 pad 11: unconnected-(U3-GPIO.3-Pad11) -> ESP_ADC1_CH6
- U3 pad 12: unconnected-(U3-RS485/GPIO.2-Pad12) -> ESP_GPIO8
- U3 pad 13: Net-(U3-RXT/GPIO.1) -> ESP_GPIO9
- U3 pad 14: Net-(U3-TXT/GPIO.0) -> ESP_GPIO10
- U3 pad 15: unconnected-(U3-~{SUSPEND}-Pad15) -> Net-(D7-A)
- U3 pad 16: Net-(U3-VPP) -> EN/UVLO
- U3 pad 19: /ESP32/RTS -> unconnected-(U3-IO15-Pad19)
- U3 pad 20: /ESP32/TXD0 -> unconnected-(U3-IO16-Pad20)
- U3 pad 21: /ESP32/RXD0 -> TPS_FAULT_INT
- U3 pad 23: /ESP32/DTR -> /ESP32/USB_D-
- U3 pad 24: unconnected-(U3-~{DCD}-Pad24) -> /ESP32/USB_D+
- U3 pad 25: GND -> GATE_DRV
- U3 pad 3: /ESP32/d+ -> +3V3
- U3 pad 4: /ESP32/d- -> /ESP32/BOOT0
- U3 pad 5: +3V3 -> unconnected-(U3-IO1-Pad5)
- U3 pad 6: +3V3 -> ESP_ADC1_CH1
- U3 pad 7: +3V3 -> ESP_ADC1_CH2
- U3 pad 8: VBUS -> ESP_ADC1_CH3
- U3 pad 9: unconnected-(U3-~{RST}-Pad9) -> ESP_ADC1_CH4
- U4 pad 1: SENSE_1A -> Net-(D8-K)
- U4 pad 2: Net-(U4A--) -> GND
- U4 pad 3: VCAP -> Net-(U4-EN)
- U4 pad 4: Net-(U4A-VCC) -> unconnected-(U4-NC-Pad4)
- U4 pad 5: Net-(U4A--) -> +3V3
- U5 pad 3: /GaN FET and Current Sensing/in+ -> GATE_DRV
- U5 pad 4: /GaN FET and Current Sensing/OUTL -> /Switching FET/OUTL
- U5 pad 5: /GaN FET and Current Sensing/OUTH -> /Switching FET/OUTH
- U5 pad 6: /GaN FET and Current Sensing/vref -> /Switching FET/vref
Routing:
- net ADC_20A: track 165.1 -> 0.00 mm, vias 5 -> 0
- net /Current Sensing/-3V3_FB: track 0.00 -> 144.0 mm, vias 0 -> 7
- net ADC_10A: track 137.9 -> 0.00 mm, vias 2 -> 0
- net GATE_DRV: track 0.00 -> 120.0 mm, vias 0 -> 4
- net VBUS: track 111.1 -> 0.00 mm, vias 1 -> 0
- net ADC_5A: track 107.3 -> 0.00 mm, vias 4 -> 0
- net GND: track 137.9 -> 243.4 mm, vias 142 -> 177
- net /GaN FET and Current Sensing/in+: track 94.2 -> 0.00 mm, vias 1 -> 0
- net /I2C Voltage Supply/VCC: track 0.00 -> 93.0 mm, vias 0 -> 5
- net ADC_1A: track 92.8 -> 0.00 mm, vias 2 -> 0
- net ESP_ADC1_CH2: track 0.00 -> 92.0 mm, vias 0 -> 2
- net Net-(RN6B-RG2): track 0.00 -> 91.7 mm, vias 0 -> 4
- net ESP_ADC1_CH5: track 0.00 -> 86.9 mm, vias 0 -> 2
- net Net-(RN6A-RG1): track 0.00 -> 86.3 mm, vias 0 -> 3
- net OPT_IN_ADC: track 73.5 -> 0.00 mm, vias 2 -> 0
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- added copper zone on F.Cu, net /I2C Voltage Supply/SW1
- added copper zone on F.Cu, net /I2C Voltage Supply/SW2
- added copper zone on F.Cu, net /I2C Voltage Supply/VOUT
- added copper zone on F.Cu, net /Switching FET/ DUT-
- added copper zone on F.Cu, net /Switching FET/DUT+
- added copper zone on F.Cu, net CS_IN
- added copper zone on F.Cu, net Net-(D1-A)
- added copper zone on F.Cu, net Net-(D1-K)
- added copper zone on F.Cu, net Net-(R16-Pad4)
- added copper zone on F.Cu, net Net-(R17-Pad4)
- added copper zone on F.Cu, net Net-(RN5B-RIN2)
- added copper zone on F.Cu, net TPS_VCAP
- added copper zone on F.Cu, net VBUS
- removed copper zone on B.Cu, net (none)
- removed copper zone on In2.Cu, net +5V
- removed copper zone on F.Cu, net /Buck Boost Supply/Vcc
- removed copper zone on F.Cu, net /Buck Boost Supply/Vout
- removed copper zone on F.Cu, net /Buck Boost Supply/tps_out
- removed copper zone on F.Cu, net /GaN FET and Current Sensing/sense_out
- removed copper zone on F.Cu, net /GaN FET and Current Sensing/vgate
- removed copper zone on F.Cu, net Net-(D5-A)
- removed copper zone on F.Cu, net Net-(U4A--)
- removed copper zone on F.Cu, net Net-(U4B--)
- removed copper zone on F.Cu, net Net-(U4C--)
- removed copper zone on F.Cu, net VCAP
- removed copper zone on F.Cu, net VCAP_EXT
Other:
- board size 127 x 96.5 mm -> 121.5 x 86 mm
- board text added: "1 2 3"
- board text added: "1-2: Ext. DUT voltage 2-3: Int. DUT voltage"
- board text added: "86 x 118 mm"
- board text added: "External Pulse Input"
- board text added: "GND GPIO10 GPIO9 GPIO8"
- board text added: "GND UART_RXD0 UART_TXD0"
- board text added: "ON OFF"
- board text added: "Optical Power Sense Input"
- board text removed: "1 3 ESP32 EXT"
- board text removed: "INT EXT"
- board text removed: "Laser Pulse Supply Rev. B Jan 2024"
- board text removed: "VBUS EXT_VIN"
